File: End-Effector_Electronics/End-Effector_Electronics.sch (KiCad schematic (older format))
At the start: 36 parts, among them J1 Raspberry_Pi_2_3, J10 SW_Push_Open, J11 SW_Push_Open, J2 LynxServo, J3 LynxServo, J4 QWIIC_Generic_Conn, J5 Conn_02x05_Odd_Even, J9 SW_Push_Open, Q1 Q_PMOS_GSD, Q2 DMMT3906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

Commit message: Started post SAR fixes
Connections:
- net +12V: now also U2.7 (SENSE+)
- net GND: now also U2.3 (VIN-)
- no-connect marks 0 -> 1
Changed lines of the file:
@@
 	8600 1050 8600 1000
 Wire Wire Line
-	8600 1000 8050 1000
+	8600 1000 8300 1000
 Wire Wire Line
 	8900 1050 8900 1000
@@
 Text Label 1000 2900 2    50   ~ 0
 LED
+Wire Wire Line
+	8050 1100 8300 1100
+Wire Wire Line
+	8300 1100 8300 1000
+Connection ~ 8300 1000
+Wire Wire Line
+	8300 1000 8050 1000
+$Comp
+L power:GND #PWR?
+U 1 1 62308E65
+P 6950 1400
+F 0 "#PWR?" H 6950 1150 50  0001 C CNN
+F 1 "GND" H 6955 1227 50  0000 C CNN
+F 2 "" H 6950 1400 50  0001 C CNN
+F 3 "" H 6950 1400 50  0001 C CNN
+	1    6950 1400
+	1    0    0    -1
+$EndComp
+Wire Wire Line
+	6950 1400 7050 1400
+NoConn ~ 8050 1300
 $EndSCHEMATC

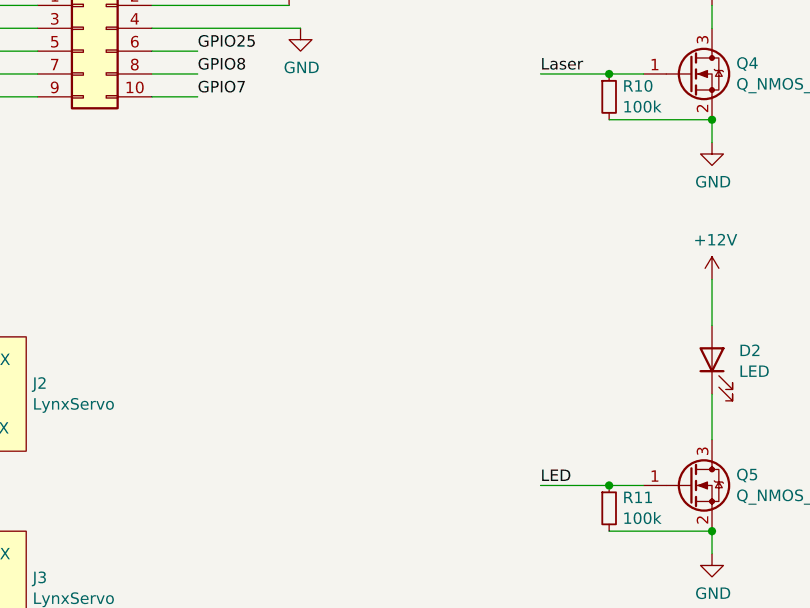
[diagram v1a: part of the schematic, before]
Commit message: indicator LEDs
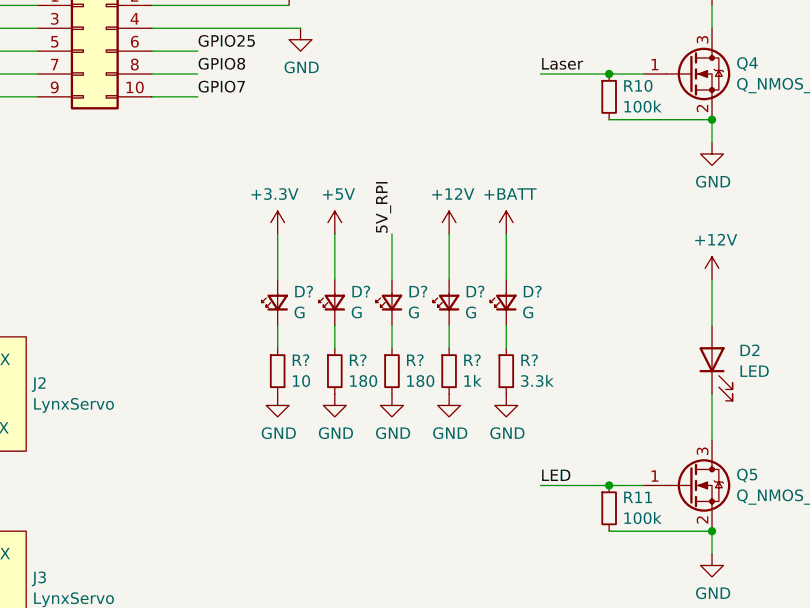
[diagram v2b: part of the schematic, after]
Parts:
- added D? (x5): G, LED_SMD:LED_0603_1608Metric_Pad1.05x0.95mm_HandSolder, symbol Device:LED_Small
- added R? (x2): 180, Resistor_SMD:R_0603_1608Metric, symbol Device:R_Small
- added R?: 10, Resistor_SMD:R_0603_1608Metric, symbol Device:R_Small
- added R?: 1k, Resistor_SMD:R_0603_1608Metric, symbol Device:R_Small
- added R?: 3.3k, Resistor_SMD:R_0603_1608Metric, symbol Device:R_Small
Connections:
- net +12V: now also D?.2 (A)
- net +3V3: now also D?.2 (A)
- net +5V: now also D?.2 (A)
- net +BATT: now also D?.2 (A)
- net 5V_RPI: now also D?.2 (A)
- net GND: now also R?.2, R?.2, R?.2, R?.2, R?.2
- new net: D?.1 (K), R?.1 (x5)

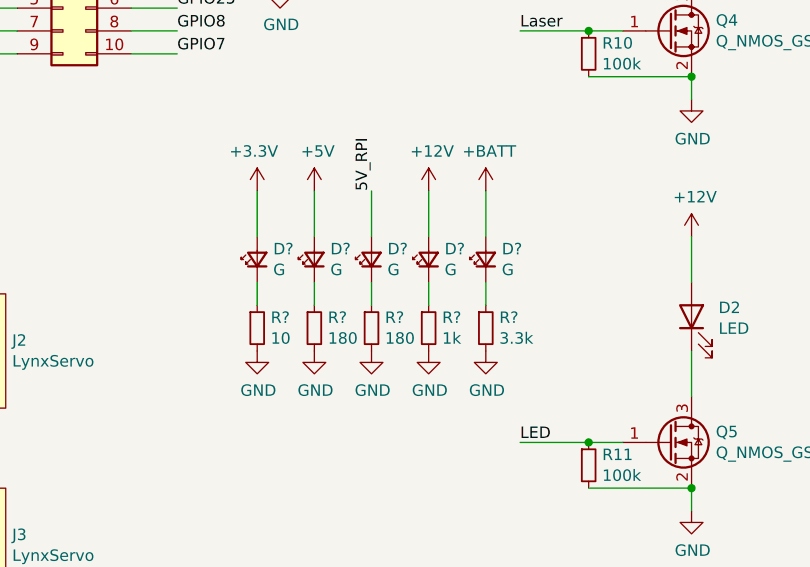
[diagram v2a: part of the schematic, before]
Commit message: Indicator LEDs in PCB
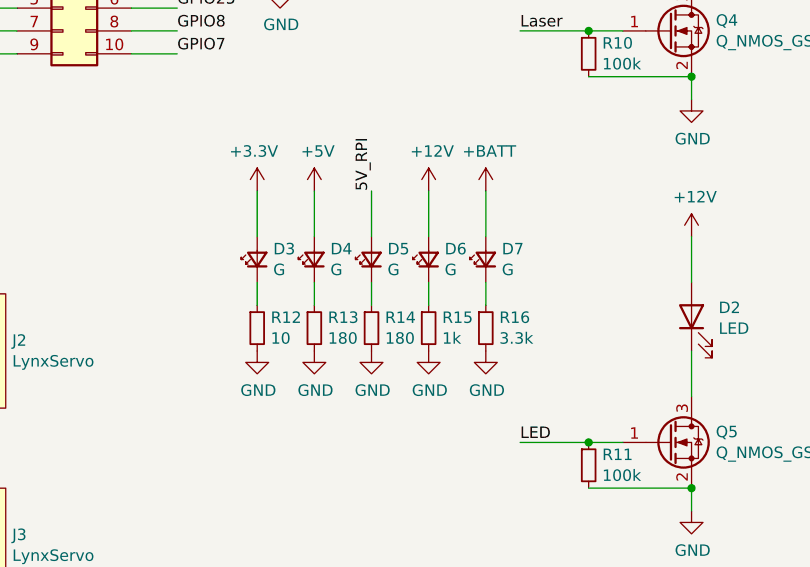
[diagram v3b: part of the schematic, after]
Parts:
- gave numbers to parts that had none: 10
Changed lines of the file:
@@
 	8300 1000 8050 1000
 $Comp
-L power:GND #PWR?
+L power:GND #PWR0102
 U 1 1 62308E65
 P 6950 1400
-F 0 "#PWR?" H 6950 1150 50  0001 C CNN
+F 0 "#PWR0102" H 6950 1150 50  0001 C CNN
 F 1 "GND" H 6955 1227 50  0000 C CNN
 F 2 "" H 6950 1400 50  0001 C CNN
@@
 NoConn ~ 8050 1300
 $Comp
-L Device:LED_Small D?
+L Device:LED_Small D4
 U 1 1 6231566C
 P 6000 4000
-F 0 "D?" V 6046 3930 50  0000 R CNN
+F 0 "D4" V 6046 3930 50  0000 R CNN
 F 1 "G" V 5955 3930 50  0000 R CNN
 F 2 "LED_SMD:LED_0603_1608Metric_Pad1.05x0.95mm_HandSolder" V 6000 4000 50  0001 C CNN
@@
 $EndComp
 $Comp
-L power:+5V #PWR?
+L power:+5V #PWR0103
 U 1 1 62317C35
 P 6000 3700
-F 0 "#PWR?" H 6000 3550 50  0001 C CNN
+F 0 "#PWR0103" H 6000 3550 50  0001 C CNN
 F 1 "+5V" H 6015 3873 50  0000 C CNN
 F 2 "" H 6000 3700 50  0001 C CNN
@@
 $EndComp
 $Comp
-L power:+3.3V #PWR?
+L power:+3.3V #PWR0104
 U 1 1 62317EC1
 P 5750 3700
-F 0 "#PWR?" H 5750 3550 50  0001 C CNN
+F 0 "#PWR0104" H 5750 3550 50  0001 C CNN
 F 1 "+3.3V" H 5765 3873 50  0000 C CNN
 F 2 "" H 5750 3700 50  0001 C CNN
@@
 $EndComp
 $Comp
-L power:+BATT #PWR?
+L power:+BATT #PWR0105
 U 1 1 6231831B
 P 6750 3700
-F 0 "#PWR?" H 6750 3550 50  0001 C CNN
+F 0 "#PWR0105" H 6750 3550 50  0001 C CNN
 F 1 "+BATT" H 6765 3873 50  0000 C CNN
 F 2 "" H 6750 3700 50  0001 C CNN
@@
 5V_RPI
 $Comp
-L power:+12V #PWR?
+L power:+12V #PWR0106
 U 1 1 62318C23
 P 6500 3700
-F 0 "#PWR?" H 6500 3550 50  0001 C CNN
+F 0 "#PWR0106" H 6500 3550 50  0001 C CNN
 F 1 "+12V" H 6515 3873 50  0000 C CNN
 F 2 "" H 6500 3700 50  0001 C CNN
@@
 $EndComp
 $Comp
-L Device:R_Small R?
+L Device:R_Small R13
 U 1 1 6231BE97
 P 6000 4300
-F 0 "R?" H 6059 4346 50  0000 L CNN
+F 0 "R13" H 6059 4346 50  0000 L CNN
 F 1 "180" H 6059 4255 50  0000 L CNN
 F 2 "Resistor_SMD:R_0603_1608Metric" H 6000 4300 50  0001 C CNN
@@
 	6000 3900 6000 3700
 $Comp
-L power:GND #PWR?
+L power:GND #PWR0107
 U 1 1 6232A93F
 P 6000 4400
-F 0 "#PWR?" H 6000 4150 50  0001 C CNN
+F 0 "#PWR0107" H 6000 4150 50  0001 C CNN
 F 1 "GND" H 6005 4227 50  0000 C CNN
 F 2 "" H 6000 4400 50  0001 C CNN
@@
 $EndComp
 $Comp
-L Device:LED_Small D?
+L Device:LED_Small D5
 U 1 1 6232AD7A
 P 6250 4000
-F 0 "D?" V 6296 3930 50  0000 R CNN
+F 0 "D5" V 6296 3930 50  0000 R CNN
 F 1 "G" V 6205 3930 50  0000 R CNN
 F 2 "LED_SMD:LED_0603_1608Metric_Pad1.05x0.95mm_HandSolder" V 6250 4000 50  0001 C CNN
@@
 $EndComp
 $Comp
-L Device:R_Small R?
+L Device:R_Small R14
 U 1 1 6232B449
 P 6250 4300
-F 0 "R?" H 6309 4346 50  0000 L CNN
+F 0 "R14" H 6309 4346 50  0000 L CNN
 F 1 "180" H 6309 4255 50  0000 L CNN
 F 2 "Resistor_SMD:R_0603_1608Metric" H 6250 4300 50  0001 C CNN
@@
 	6250 3900 6250 3700
 $Comp
-L power:GND #PWR?
+L power:GND #PWR0108
 U 1 1 6232B455
 P 6250 4400
-F 0 "#PWR?" H 6250 4150 50  0001 C CNN
+F 0 "#PWR0108" H 6250 4150 50  0001 C CNN
 F 1 "GND" H 6255 4227 50  0000 C CNN
 F 2 "" H 6250 4400 50  0001 C CNN
@@
 $EndComp
 $Comp
-L Device:LED_Small D?
+L Device:LED_Small D3
 U 1 1 62334908
 P 5750 4000
-F 0 "D?" V 5796 3930 50  0000 R CNN
+F 0 "D3" V 5796 3930 50  0000 R CNN
 F 1 "G" V 5705 3930 50  0000 R CNN
 F 2 "LED_SMD:LED_0603_1608Metric_Pad1.05x0.95mm_HandSolder" V 5750 4000 50  0001 C CNN
@@
 $EndComp
 $Comp
-L Device:R_Small R?
+L Device:R_Small R12
 U 1 1 6233490F
 P 5750 4300
-F 0 "R?" H 5809 4346 50  0000 L CNN
+F 0 "R12" H 5809 4346 50  0000 L CNN
 F 1 "10" H 5809 4255 50  0000 L CNN
 F 2 "Resistor_SMD:R_0603_1608Metric" H 5750 4300 50  0001 C CNN
@@
 	5750 3900 5750 3700
 $Comp
-L power:GND #PWR?
+L power:GND #PWR0109
 U 1 1 62334917
 P 5750 4400
-F 0 "#PWR?" H 5750 4150 50  0001 C CNN
+F 0 "#PWR0109" H 5750 4150 50  0001 C CNN
 F 1 "GND" H 5755 4227 50  0000 C CNN
 F 2 "" H 5750 4400 50  0001 C CNN
@@
 $EndComp
 $Comp
-L Device:LED_Small D?
+L Device:LED_Small D6
 U 1 1 6233BC2E
 P 6500 4000
-F 0 "D?" V 6546 3930 50  0000 R CNN
+F 0 "D6" V 6546 3930 50  0000 R CNN
 F 1 "G" V 6455 3930 50  0000 R CNN
 F 2 "LED_SMD:LED_0603_1608Metric_Pad1.05x0.95mm_HandSolder" V 6500 4000 50  0001 C CNN
@@
 $EndComp
 $Comp
-L Device:R_Small R?
+L Device:R_Small R15
 U 1 1 6233BC35
 P 6500 4300
-F 0 "R?" H 6559 4346 50  0000 L CNN
+F 0 "R15" H 6559 4346 50  0000 L CNN
 F 1 "1k" H 6559 4255 50  0000 L CNN
 F 2 "Resistor_SMD:R_0603_1608Metric" H 6500 4300 50  0001 C CNN
@@
 	6500 3900 6500 3700
 $Comp
-L power:GND #PWR?
+L power:GND #PWR0110
 U 1 1 6233BC3D
 P 6500 4400
-F 0 "#PWR?" H 6500 4150 50  0001 C CNN
+F 0 "#PWR0110" H 6500 4150 50  0001 C CNN
 F 1 "GND" H 6505 4227 50  0000 C CNN
 F 2 "" H 6500 4400 50  0001 C CNN
@@
 $EndComp
 $Comp
-L Device:LED_Small D?
+L Device:LED_Small D7
 U 1 1 62342FBC
 P 6750 4000
-F 0 "D?" V 6796 3930 50  0000 R CNN
+F 0 "D7" V 6796 3930 50  0000 R CNN
 F 1 "G" V 6705 3930 50  0000 R CNN
 F 2 "LED_SMD:LED_0603_1608Metric_Pad1.05x0.95mm_HandSolder" V 6750 4000 50  0001 C CNN
@@
 $EndComp
 $Comp
-L Device:R_Small R?
+L Device:R_Small R16
 U 1 1 62342FC3
 P 6750 4300
-F 0 "R?" H 6809 4346 50  0000 L CNN
+F 0 "R16" H 6809 4346 50  0000 L CNN
 F 1 "3.3k" H 6809 4255 50  0000 L CNN
 F 2 "Resistor_SMD:R_0603_1608Metric" H 6750 4300 50  0001 C CNN
@@
 	6750 3900 6750 3700
 $Comp
-L power:GND #PWR?
+L power:GND #PWR0111
 U 1 1 62342FCB
 P 6750 4400
-F 0 "#PWR?" H 6750 4150 50  0001 C CNN
+F 0 "#PWR0111" H 6750 4150 50  0001 C CNN
 F 1 "GND" H 6755 4227 50  0000 C CNN
 F 2 "" H 6750 4400 50  0001 C CNN
